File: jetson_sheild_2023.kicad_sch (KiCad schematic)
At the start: 19 parts, among them IC1 TJA1441AT_0Z, J1 JetsonOrinNano_DevKit_J12, J10 BlockDetectLimSw_Rear, J2 VL53L1X_front, J3 VL53L1X_middle, J4 VL53L1X_rear, J5 BlockDetectLimSw_Front, J6 BlockDetectLimSw_MiddleOn, J7 BlockDetectLimSw_MiddleOff, J8 Conn_01x04_Socket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

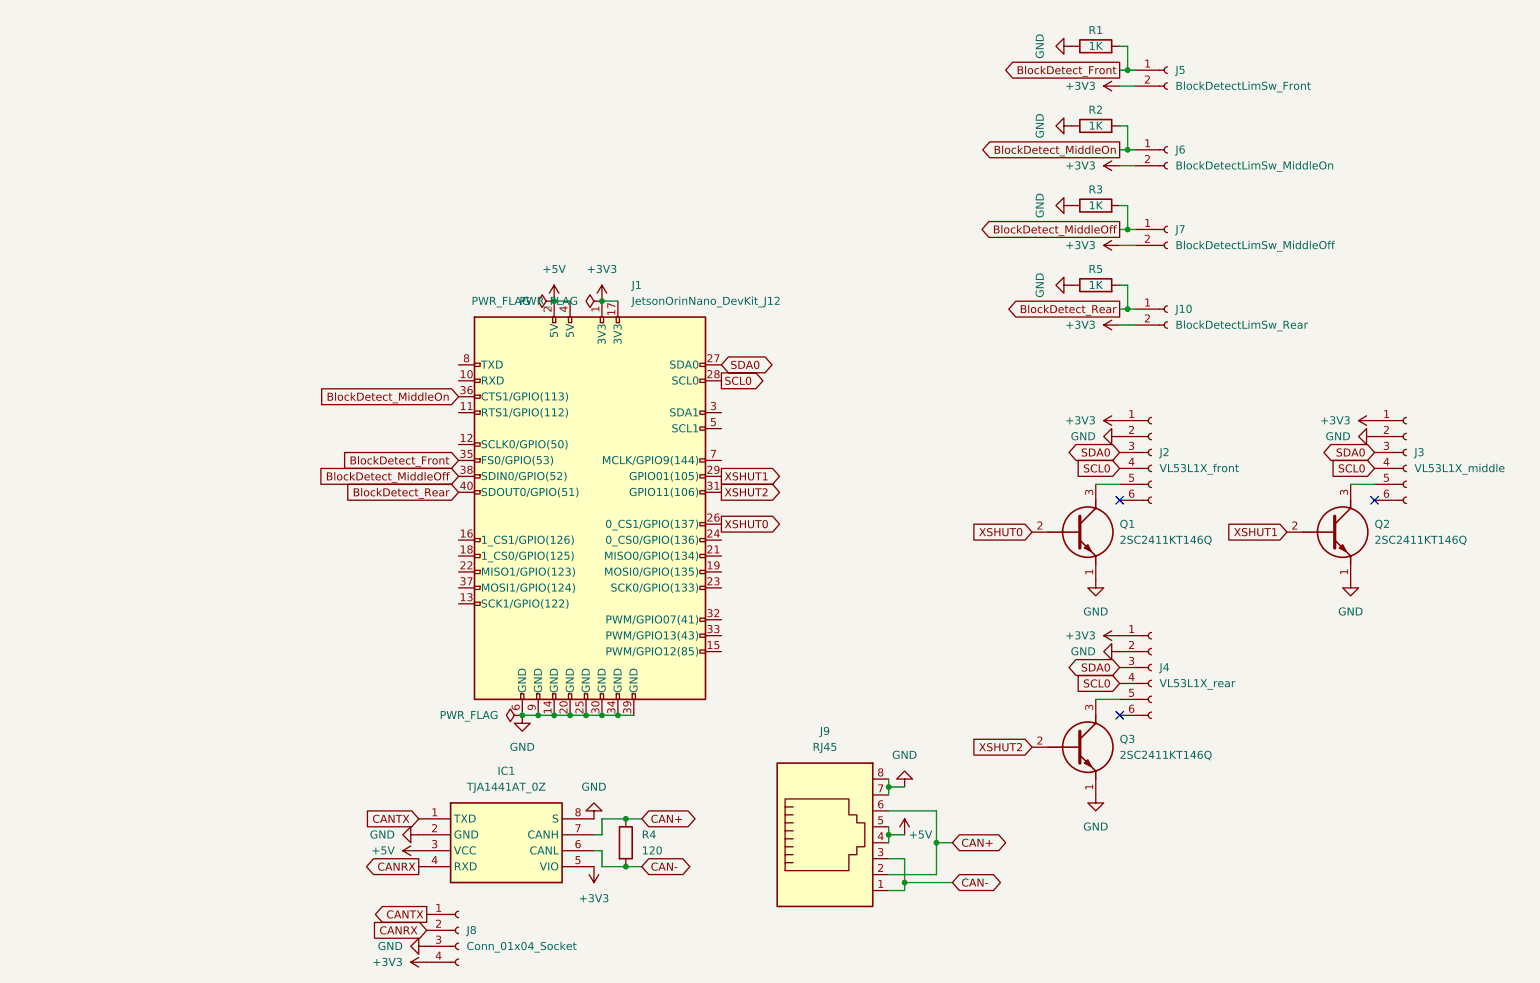
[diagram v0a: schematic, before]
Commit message: ZHコネクタをPHコネクタに変更,電源ボタンと汎用ボタンを追加,バージョンとロゴを印字
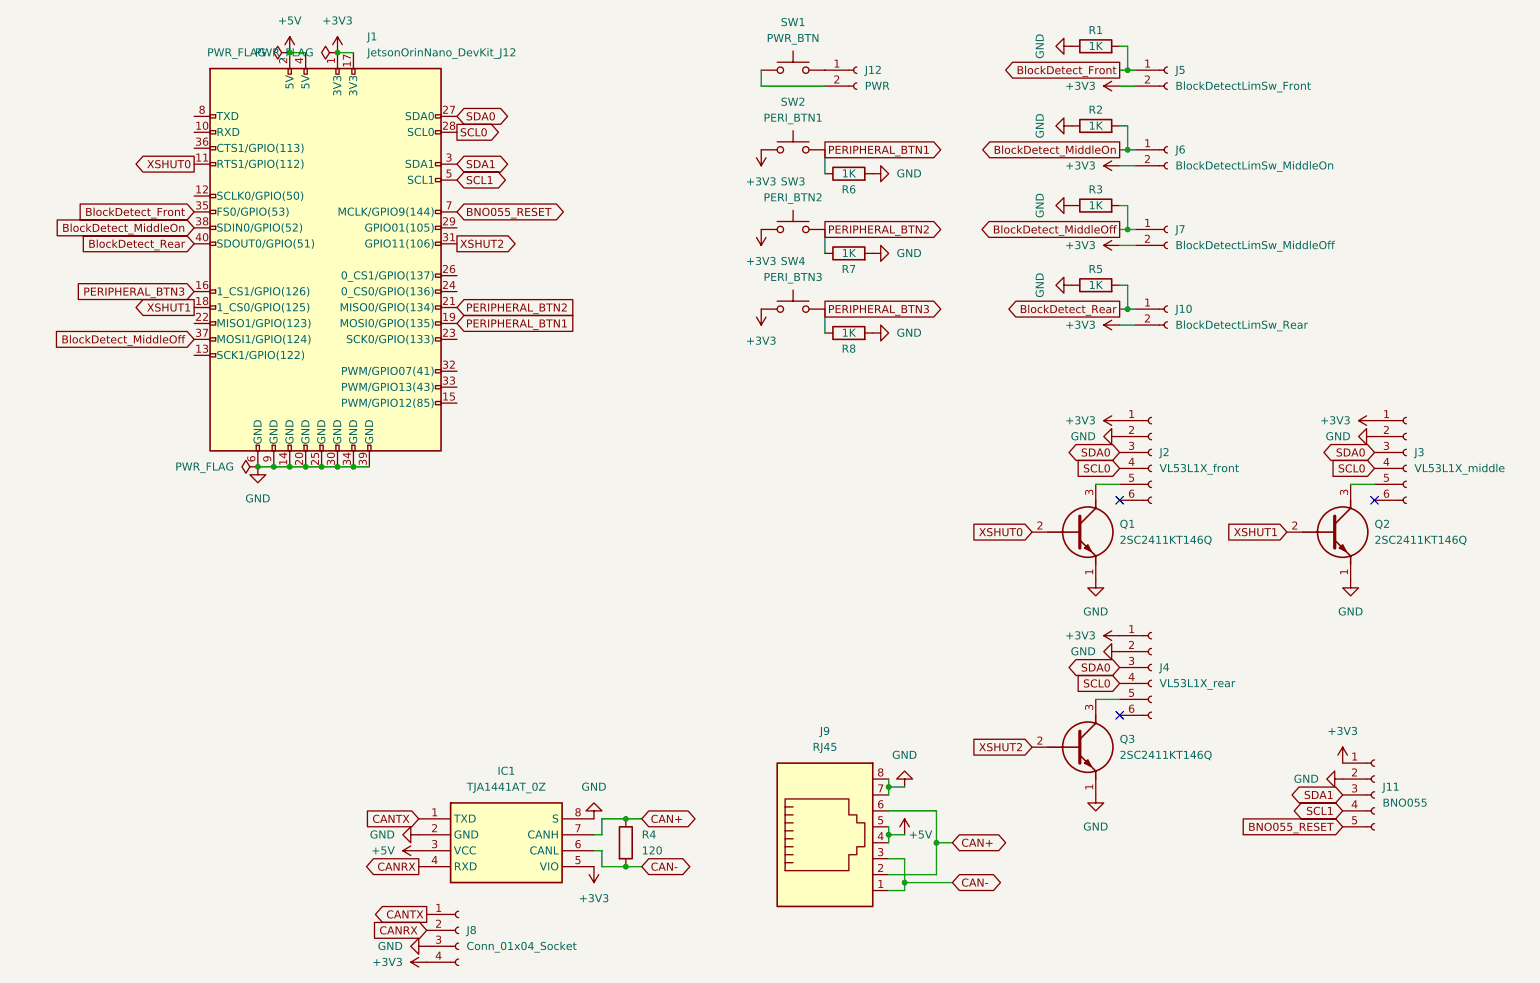
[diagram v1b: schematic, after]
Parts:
- added J11: BNO055, Connector_JST:JST_PH_S5B-PH-K_1x05_P2.00mm_Horizontal, symbol Connector:Conn_01x05_Socket
- added J12: PWR, Connector_JST:JST_XH_B2B-XH-A_1x02_P2.50mm_Vertical, symbol Connector:Conn_01x02_Socket
- added R6, R7, R8: 1K, Resistor_SMD:R_0603_1608Metric_Pad0.98x0.95mm_HandSolder, symbol Device:R
- added SW1: PWR_BTN, Button_Switch_SMD:SW_SPST_PTS645, symbol Switch:SW_Push
- added SW2: PERI_BTN1, Button_Switch_SMD:SW_SPST_PTS645, symbol Switch:SW_Push
- added SW3: PERI_BTN2, Button_Switch_SMD:SW_SPST_PTS645, symbol Switch:SW_Push
- added SW4: PERI_BTN3, Button_Switch_SMD:SW_SPST_PTS645, symbol Switch:SW_Push
- J2, J3, J4: footprint samacsys_lib:SHDRRA6W50P0X150_1X6_1050X600X370P -> Connector_JST:JST_PH_S6B-PH-K_1x06_P2.00mm_Horizontal
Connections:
- net +3V3: now also J11.1 (Pin_1), SW2.1, SW3.1, SW4.1
- net BlockDetect_MiddleOff: now also J1.37 (MOSI1/GPIO(124)); no longer J1.38 (SDIN0/GPIO(52))
- net BlockDetect_MiddleOn: now also J1.38 (SDIN0/GPIO(52)); no longer J1.36 (CTS1/GPIO(113))
- net GND: now also J11.2 (Pin_2), R6.2, R7.2, R8.2
- net XSHUT0: now also J1.11 (RTS1/GPIO(112)); no longer J1.26 (0_CS1/GPIO(137))
- net XSHUT1: now also J1.18 (1_CS0/GPIO(125)); no longer J1.29 (GPIO01(105))
- net PERIPHERAL_BTN3: now reaches J1.16 (1_CS1/GPIO(126))
- net PERIPHERAL_BTN3: now also R8.1, SW4.2
- net PERIPHERAL_BTN1: now reaches J1.19 (MOSI0/GPIO(135))
- net PERIPHERAL_BTN1: now also R6.1, SW2.2
- net PERIPHERAL_BTN2: now reaches J1.21 (MISO0/GPIO(134))
- net PERIPHERAL_BTN2: now also R7.1, SW3.2
- net SDA1: now reaches J1.3 (SDA1)
- net SDA1: now also J11.3 (Pin_3)
- net SCL1: now reaches J1.5 (SCL1)
- net SCL1: now also J11.4 (Pin_4)
- net BNO055_RESET: now reaches J1.7 (MCLK/GPIO9(144))
- net BNO055_RESET: now also J11.5 (Pin_5)
- new net: J12.2 (Pin_2), SW1.1
- new net: J12.1 (Pin_1), SW1.2
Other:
- moved on the sheet: J1
